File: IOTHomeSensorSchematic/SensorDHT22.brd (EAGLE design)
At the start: 100 x 80 mm, 20 parts, among them J1 AVR_SPI_PRG_6NS, J2 FTDI_BASICPTH, Q1 MOSFET-NCHANNELFQP30N06L, U1 ATMEGA328P_PDIP, U3 RFM69HW

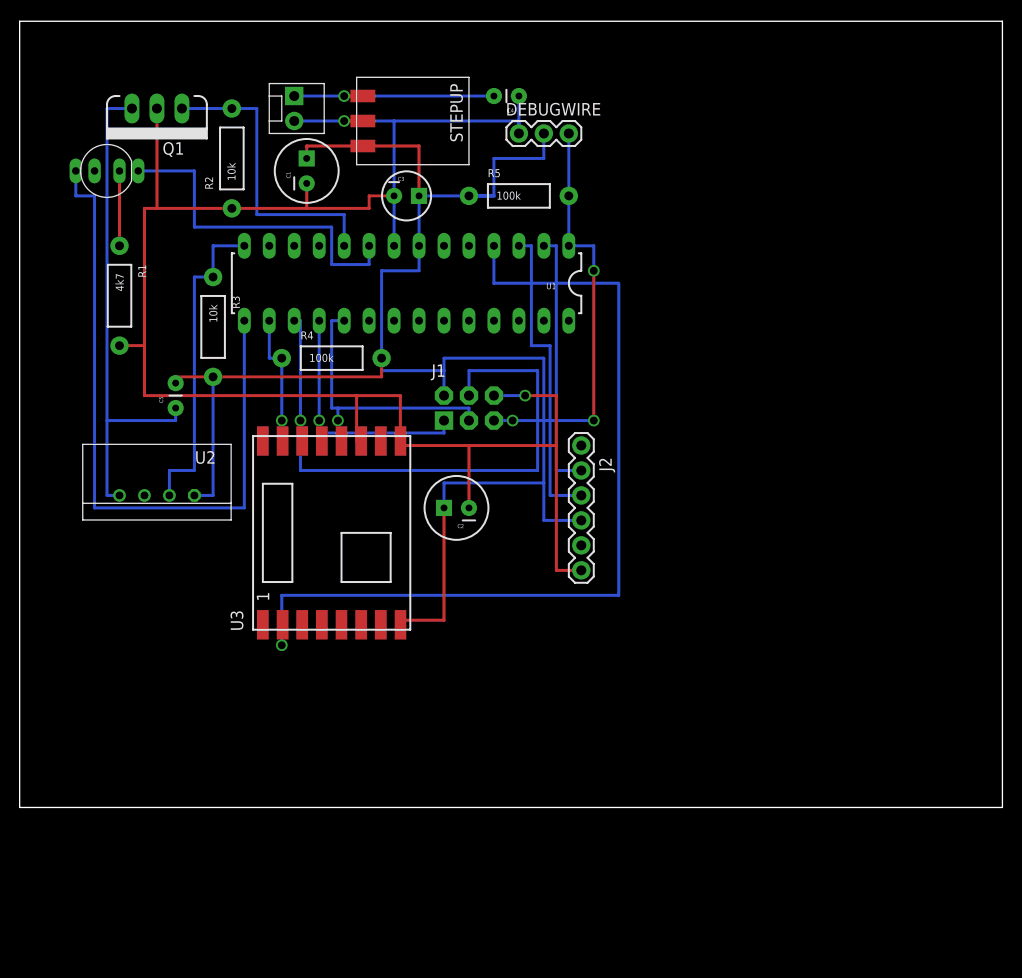
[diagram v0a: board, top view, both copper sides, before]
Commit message: Added schematic PCB design
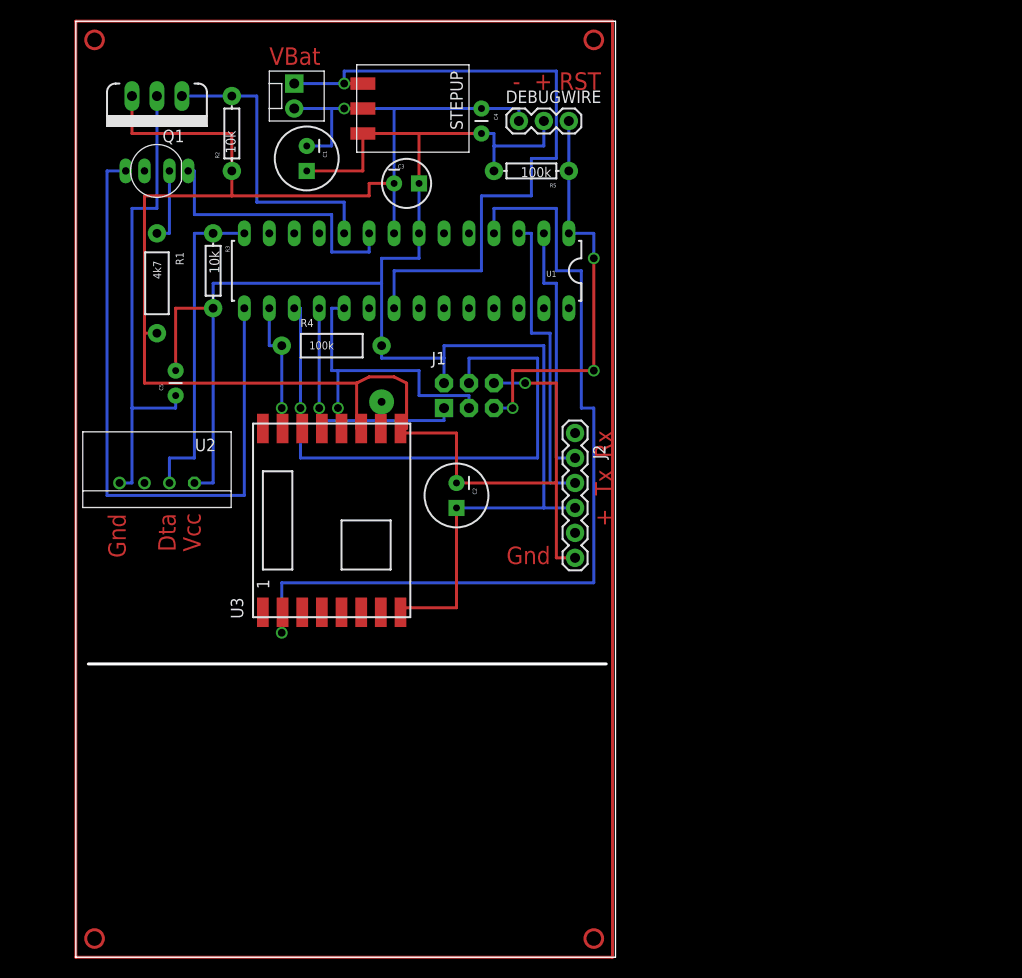
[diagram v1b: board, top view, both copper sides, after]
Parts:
- R2, R3, R5: device SparkFun-Passives:AXIAL-0.4 -> SparkFun-Resistors:AXIAL-0.3
- moved R3 5.71 mm to (19.7, 54.6)
- moved D1 5.08 mm to (14.0, 64.8)
- moved R1 4.02 mm to (14.0, 53.3)
- moved C4 4.02 mm to (47.0, 71.1), turned to 270 degrees
- moved R5 2.84 mm to (52.1, 64.8), turned to 180 degrees
- moved R2 2.54 mm to (21.6, 68.6)
- moved J2 1.42 mm to (56.5, 38.1)
- moved C1 1.27 mm to (29.2, 66.0), turned to 270 degrees
- moved STEPUP 1.27 mm to (35.6, 71.1)
- moved C3 1.27 mm to (39.4, 63.5)
- moved R4 1.27 mm to (31.8, 47.0)
- moved U2 1.27 mm to (14.0, 33.0)
- moved C2 1.27 mm to (44.5, 31.8), turned to 270 degrees
- moved U3 1.27 mm to (31.8, 29.2)
- moved C5 1.27 mm to (15.9, 41.9)
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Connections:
- net N$1: now also C1.2, C2.2, C3.2, C4.1, DEBUGWIRE.1, J1.6, J2.GND, J3.2, R1.P$2, R2.P$1, STEPUP.GND, U1.8, U3.11, U3.9; no longer C5.1, U2.GND
- net N$15: now also R5.P$1; no longer R5.P$2
- net N$16: now also C4.2, R5.P$2; no longer R5.P$1
- net N$2: now also U1.21; no longer C4.2
- net N$3: now also C5.1, U2.GND; no longer C1.2, C2.2, C3.2, C4.1, DEBUGWIRE.1, J1.6, J2.GND, J3.2, R1.P$2, R2.P$1, STEPUP.GND, U1.8, U3.11, U3.9
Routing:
- net N$28: track 0.00 -> 299.7 mm
- net N$1: track 51.4 -> 196.9 mm
- net N$3: track 188.3 -> 48.9 mm
- net N$2: track 22.2 -> 70.5 mm
- net N$16: track 165.3 -> 175.4 mm
- net N$11: track 34.9 -> 28.6 mm
- net N$17: track 29.1 -> 31.7 mm
- net N$10: track 70.5 -> 67.9 mm
- net N$7: track 26.7 -> 26.0 mm
- net N$4: track 31.8 -> 31.1 mm
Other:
- board size 100 x 80 mm -> 54.9 x 95.2 mm
- board text added: "+"
- board text added: "- + RST"
- board text added: "Dta"
- board text added: "Gnd"
- board text added: "Rx"
- board text added: "Tx"
- board text added: "VBat"
- board text added: "Vcc"
